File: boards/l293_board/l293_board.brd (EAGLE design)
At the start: 32.7 x 25.4 mm, 7 parts, among them IC1 L293D

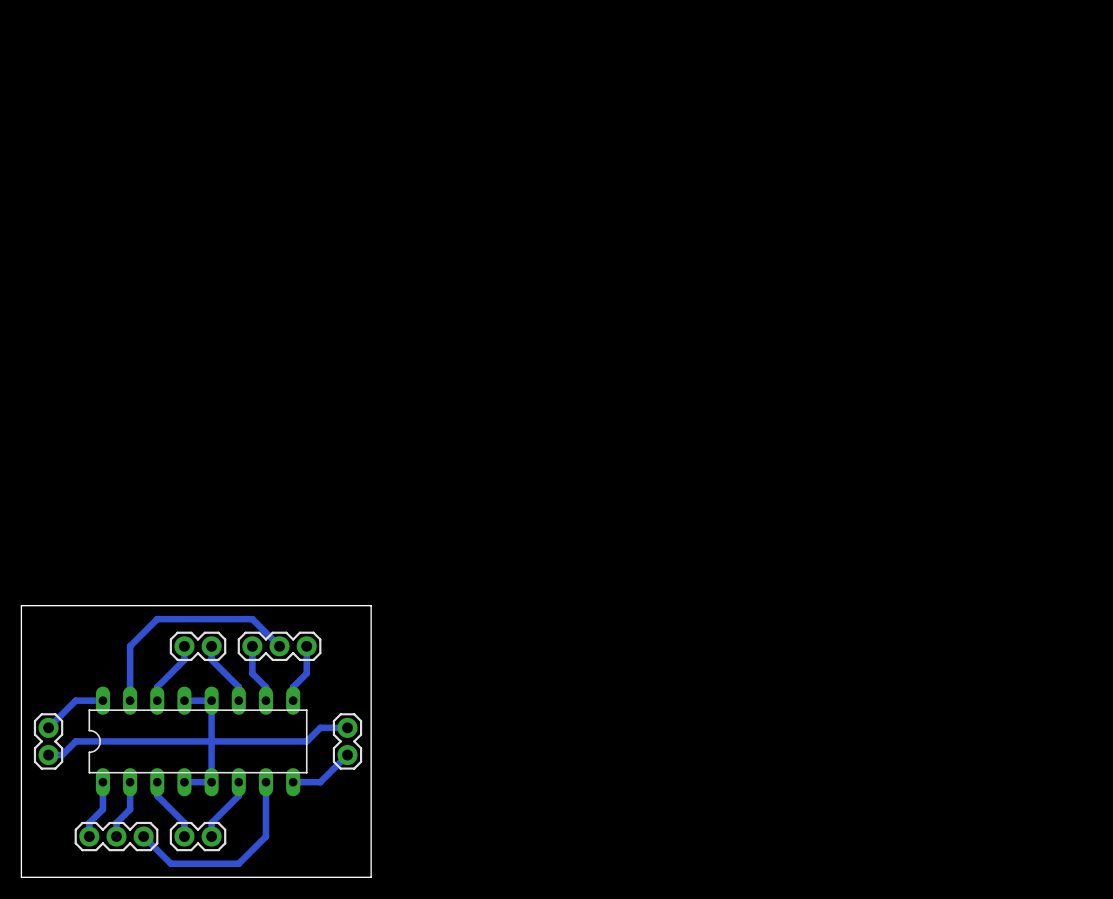
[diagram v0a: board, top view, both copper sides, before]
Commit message: updated board to make 5x2 connector
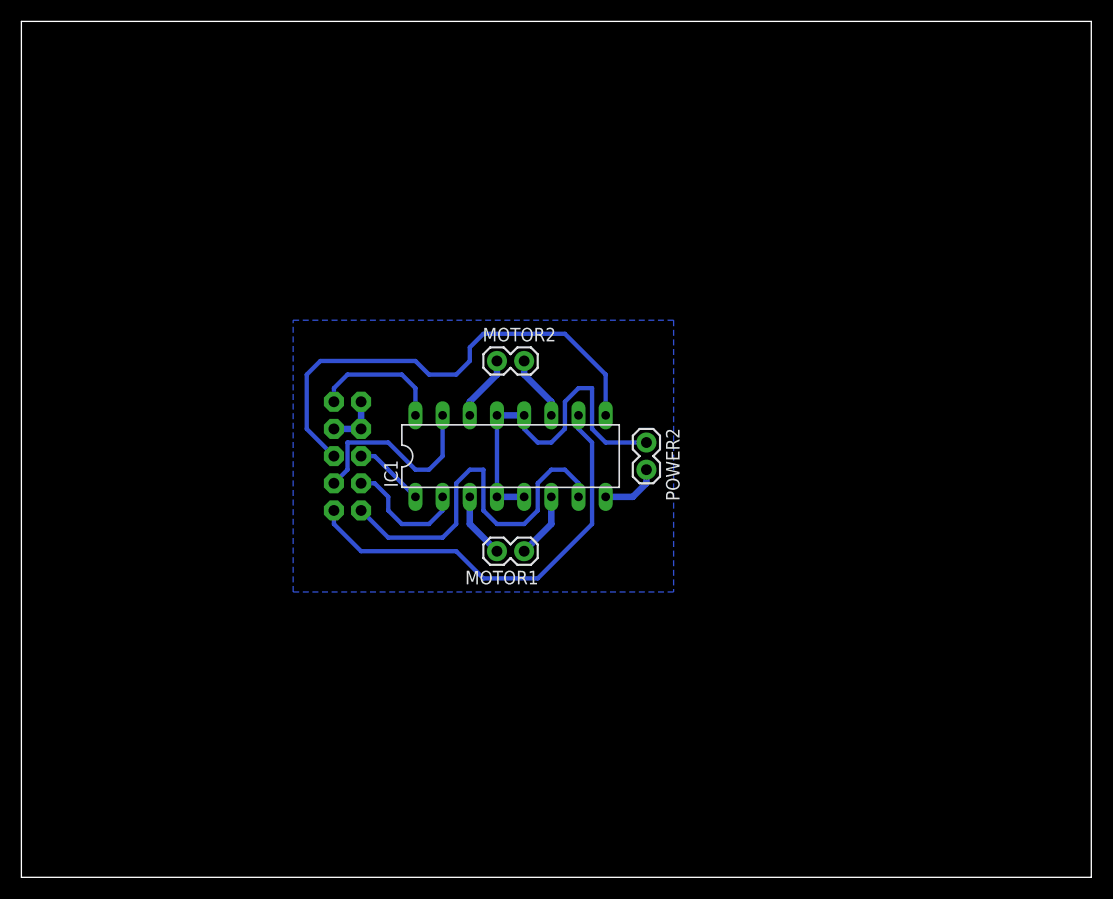
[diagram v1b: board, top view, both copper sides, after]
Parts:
- removed CON_MOTOR1, CON_MOTOR2: (no value), SparkFun-Connectors:1X03
- removed POWER1: M02PTH, SparkFun-Connectors:1X02
- added JP1: M05X2NO_SILK, SparkFun-Connectors:2X5_NOSILK
- moved MOTOR1 39.6 mm to (47.0, 30.5)
- moved IC1 39.6 mm to (45.7, 39.4)
- moved MOTOR2 39.6 mm to (44.5, 48.3)
- moved POWER2 38.6 mm to (58.4, 40.6)
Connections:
- net GND: now also JP1.1, JP1.3, JP1.4; no longer POWER1.1
- net N$1: now also JP1.6; no longer CON_MOTOR2.1
- net N$11: now also JP1.10; no longer CON_MOTOR2.3
- net N$2: now also JP1.5; no longer CON_MOTOR1.3
- net N$5: now also JP1.8; no longer CON_MOTOR2.2
- net N$6: now also JP1.7; no longer CON_MOTOR1.2
- net N$7: now also JP1.9; no longer CON_MOTOR1.1
- net VCC: now also JP1.2; no longer POWER1.2
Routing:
- net N$1: track 5.61 -> 45.4 mm
- net N$11: track 5.61 -> 40.3 mm
- net N$7: track 18.6 -> 36.0 mm
- net VCC: track 6.13 -> 12.5 mm
- net N$6: track 5.61 -> 11.7 mm
- net GND: track 41.7 -> 38.9 mm
- net N$5: track 21.2 -> 18.6 mm
- net N$2: track 5.61 -> 6.66 mm
- net VSS: track 6.13 -> 5.61 mm
- added copper zone on layer 16, net GND
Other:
- board size 32.7 x 25.4 mm -> 100 x 80 mm
